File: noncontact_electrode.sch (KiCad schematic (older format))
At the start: 10 parts, among them J1 CONN_01, J2 CONN_01, U1 LMP7702MM

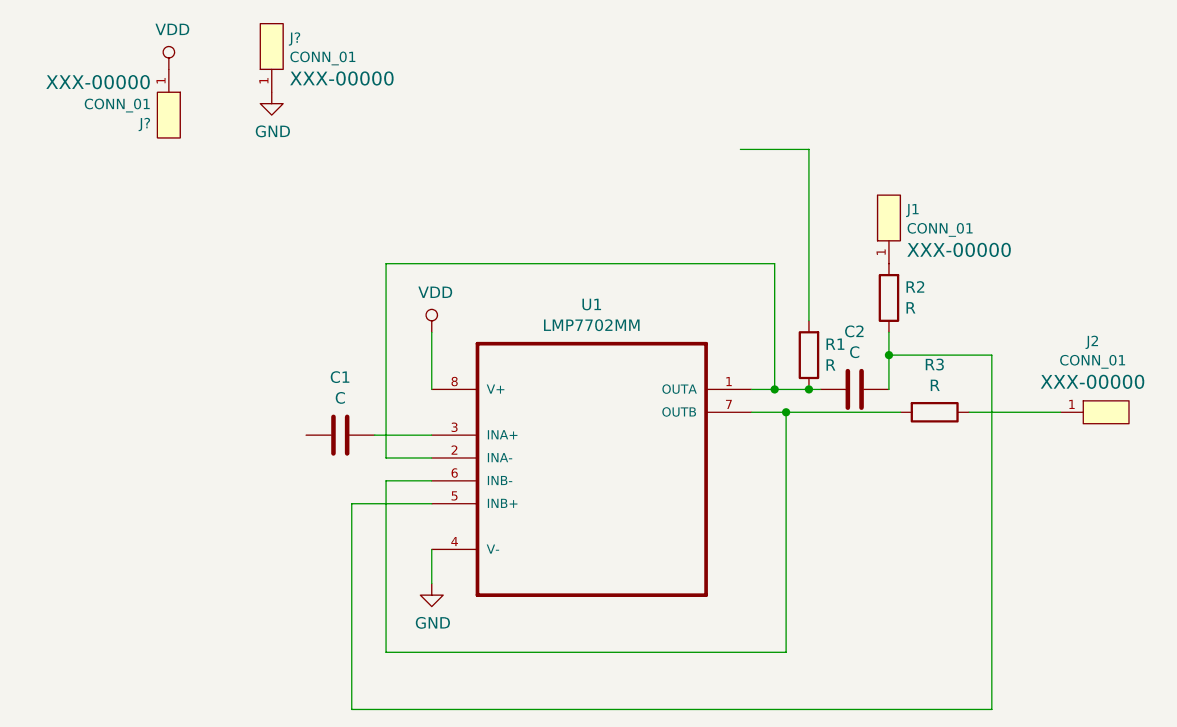
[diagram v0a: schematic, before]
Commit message: B paste and mask added
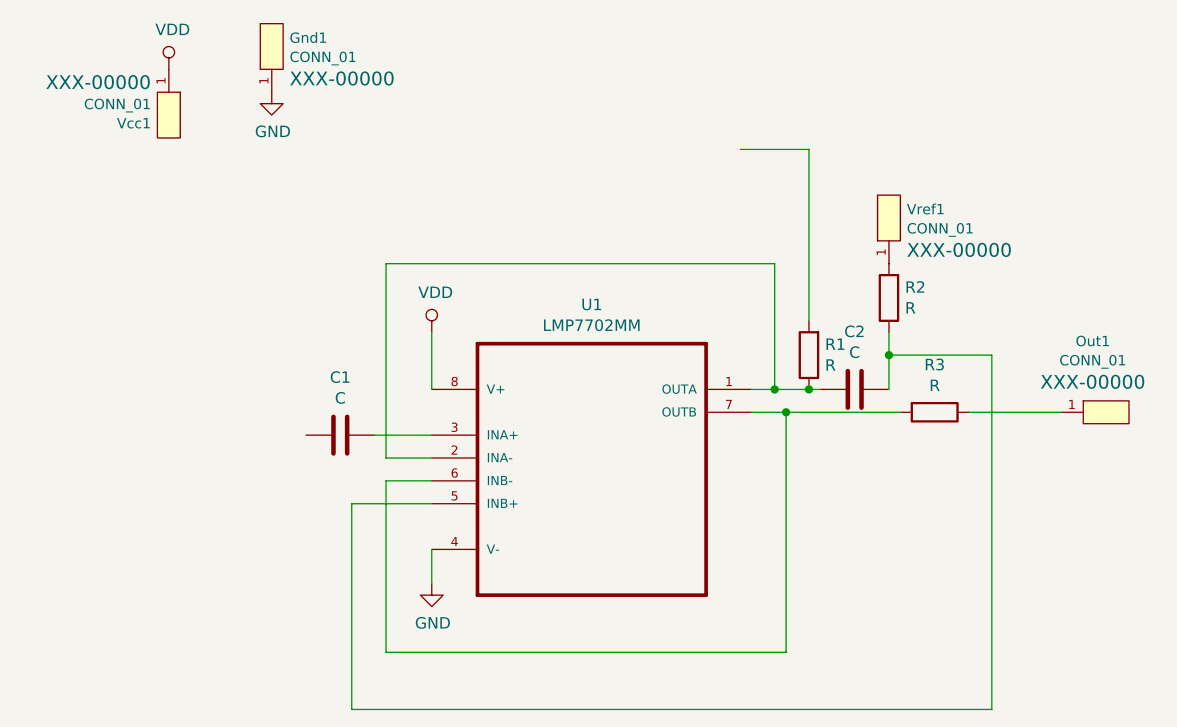
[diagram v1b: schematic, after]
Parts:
- gave numbers to parts that had none: 2
- renumbered J2 to Out1, J1 to Vref1
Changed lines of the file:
@@
 $EndComp
 $Comp
-L SparkFun-Connectors:CONN_01 J1
+L SparkFun-Connectors:CONN_01 Vref1
 U 1 1 5D4DD422
 P 6150 3450
-F 0 "J1" V 6013 3528 45  0000 L CNN
+F 0 "Vref1" V 6013 3528 45  0000 L CNN
 F 1 "CONN_01" V 6097 3528 45  0000 L CNN
 F 2 "digikey-footprints:PROBE_PAD_0603" H 6150 3650 20  0001 C CNN
@@
 	6150 3950 6150 4100
 $Comp
-L SparkFun-Connectors:CONN_01 J2
+L SparkFun-Connectors:CONN_01 Out1
 U 1 1 5D4E4202
 P 7000 4200
-F 0 "J2" H 6958 3890 45  0000 C CNN
+F 0 "Out1" H 6958 3890 45  0000 C CNN
 F 1 "CONN_01" H 6958 3974 45  0000 C CNN
 F 2 "digikey-footprints:PROBE_PAD_0603" H 7000 4400 20  0001 C CNN
@@
 $EndComp
 $Comp
-L SparkFun-Connectors:CONN_01 J?
+L SparkFun-Connectors:CONN_01 Vcc1
 U 1 1 5D4D4769
 P 3000 2800
-F 0 "J?" V 2863 2878 45  0000 L CNN
+F 0 "Vcc1" V 2863 2878 45  0000 L CNN
 F 1 "CONN_01" V 2947 2878 45  0000 L CNN
 F 2 "digikey-footprints:PROBE_PAD_0603" H 3000 3000 20  0001 C CNN
@@
 $EndComp
 $Comp
-L SparkFun-Connectors:CONN_01 J?
+L SparkFun-Connectors:CONN_01 Gnd1
 U 1 1 5D4D5D37
 P 3450 2700
-F 0 "J?" V 3313 2778 45  0000 L CNN
+F 0 "Gnd1" V 3313 2778 45  0000 L CNN
 F 1 "CONN_01" V 3397 2778 45  0000 L CNN
 F 2 "digikey-footprints:PROBE_PAD_0603" H 3450 2900 20  0001 C CNN
